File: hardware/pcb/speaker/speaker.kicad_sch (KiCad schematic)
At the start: 64 parts, among them J1 Conn_01x03, J2 Conn_01x03, J3 Conn_01x03, J4 Conn_01x03, J5 Conn_01x03, J6 Conn_01x03, J7 Conn_01x02, M1 Ultrasonic_Transducer, M10 Ultrasonic_Transducer, M11 Ultrasonic_Transducer, M12 Ultrasonic_Transducer, M13 Ultrasonic_Transducer, M14 Ultrasonic_Transducer, M15 Ultrasonic_Transducer, M16 Ultrasonic_Transducer, M17 Ultrasonic_Transducer, M18 Ultrasonic_Transducer, M19 Ultrasonic_Transducer, M2 Ultrasonic_Transducer, M3 Ultrasonic_Transducer, M4 Ultrasonic_Transducer, M5 Ultrasonic_Transducer, M6 Ultrasonic_Transducer, M7 Ultrasonic_Transducer, M8 Ultrasonic_Transducer, M9 Ultrasonic_Transducer, Q1 BC847, Q2 BC857, U1 LTC2640-Z, U2 LM2735XMF

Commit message: UPDATE BOM
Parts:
- C3: footprint Capacitor_SMD:C_0805_2012Metric_Pad1.18x1.45mm_HandSolder -> Capacitor_SMD:C_1206_3216Metric_Pad1.33x1.80mm_HandSolder
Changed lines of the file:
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@@
       (effects (font (size 1.27 1.27)) (justify left))
     )
-    (property "Footprint" "Capacitor_SMD:C_0805_2012Metric_Pad1.18x1.45mm_HandSolder" (id 2) (at 228.9302 44.45 0)
+    (property "Footprint" "Capacitor_SMD:C_1206_3216Metric_Pad1.33x1.80mm_HandSolder" (id 2) (at 228.9302 44.45 0)
       (effects (font (size 1.27 1.27)) hide)
     )
@@
     )
     (path "/892dde4e-ed28-44fe-b351-6562be659b5d"
-      (reference "C3") (unit 1) (value "10uF") (footprint "Capacitor_SMD:C_0805_2012Metric_Pad1.18x1.45mm_HandSolder")
+      (reference "C3") (unit 1) (value "10uF") (footprint "Capacitor_SMD:C_1206_3216Metric_Pad1.33x1.80mm_HandSolder")
     )
     (path "/00c022b6-5651-4944-967b-0fe8d06eb7e0"

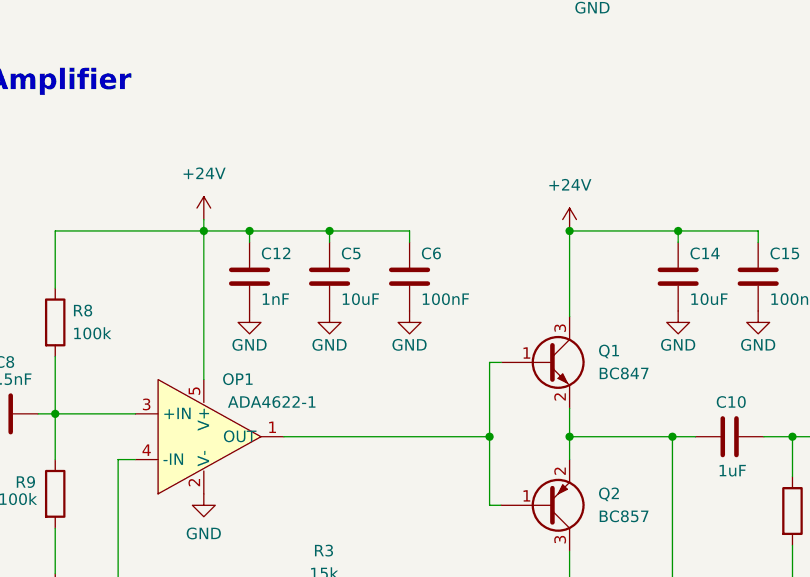
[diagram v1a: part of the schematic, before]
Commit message: rework pcb mount model
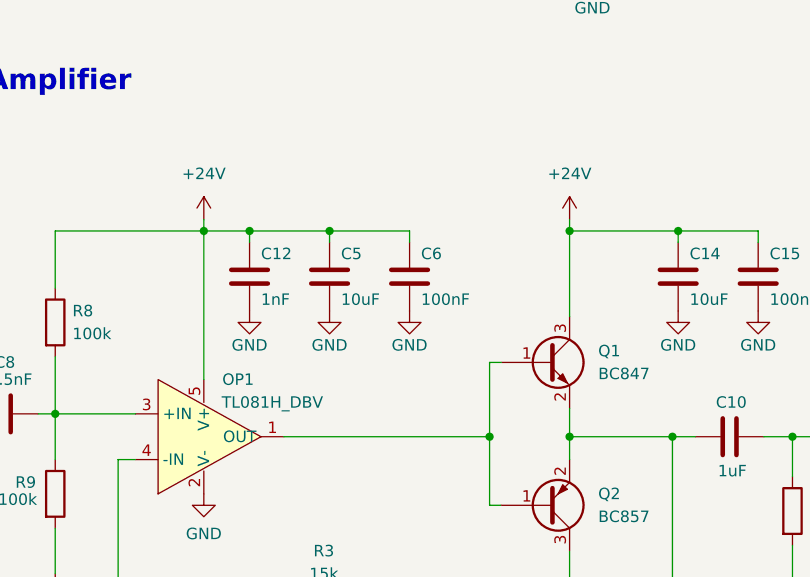
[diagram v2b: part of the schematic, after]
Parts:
- OP1: value ADA4622-1 -> TL081H_DBV
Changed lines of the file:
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@@
+    (stroke (width 0) (type default) (color 0 0 0 0))
+  )
+  (wire (pts (xy 92.075 94.615) (xy 92.075 95.885))
     (stroke (width 0) (type default) (color 0 0 0 0))
   )
@@
     (pin "1")
   )
-  (symbol (lib_id "power:+24V") (at 92.075 95.885 0) (unit 1)
-    (in_bom yes) (on_board yes) (fields_autoplaced)
-    (property "Reference" "#PWR01" (id 0) (at 92.075 99.695 0)
-      (effects (font (size 1.27 1.27)) hide)
-    )
-    (property "Value" "+24V" (id 1) (at 92.075 90.805 0))
-    (property "Footprint" "" (id 2) (at 92.075 95.885 0)
-      (effects (font (size 1.27 1.27)) hide)
-    )
-    (property "Datasheet" "" (id 3) (at 92.075 95.885 0)
+  (symbol (lib_id "power:+24V") (at 92.075 94.615 0) (unit 1)
+    (in_bom yes) (on_board yes) (fields_autoplaced)
+    (property "Reference" "#PWR01" (id 0) (at 92.075 98.425 0)
+      (effects (font (size 1.27 1.27)) hide)
+    )
+    (property "Value" "+24V" (id 1) (at 92.075 89.535 0))
+    (property "Footprint" "" (id 2) (at 92.075 94.615 0)
+      (effects (font (size 1.27 1.27)) hide)
+    )
+    (property "Datasheet" "" (id 3) (at 92.075 94.615 0)
       (effects (font (size 1.27 1.27)) hide)
     )
@@
     (in_bom yes) (on_board yes)
     (property "Reference" "OP1" (id 0) (at 55.245 112.395 0))
-    (property "Value" "ADA4622-1" (id 1) (at 59.055 114.935 0))
+    (property "Value" "TL081H_DBV" (id 1) (at 59.055 114.935 0))
     (property "Footprint" "Package_TO_SOT_SMD:SOT-23-5_HandSoldering" (id 2) (at 51.435 118.745 0)
       (effects (font (size 1.27 1.27)) hide)
@@
     )
     (path "/bf724a73-ae1d-4c58-a50e-18191201ed32"
-      (reference "OP1") (unit 1) (value "ADA4622-1") (footprint "Package_TO_SOT_SMD:SOT-23-5_HandSoldering")
+      (reference "OP1") (unit 1) (value "TL081H_DBV") (footprint "Package_TO_SOT_SMD:SOT-23-5_HandSoldering")
     )
     (path "/a413879d-4165-41a0-9ee5-56c96b82c853"

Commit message: test software
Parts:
- R4: value 5k -> 5.1k
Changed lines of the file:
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@@
       (effects (font (size 1.27 1.27)) (justify left))
     )
-    (property "Value" "5k" (id 1) (at 44.45 144.7799 0)
+    (property "Value" "5.1k" (id 1) (at 44.45 144.7799 0)
       (effects (font (size 1.27 1.27)) (justify left))
     )
@@
     )
     (path "/1392ace3-2479-46d2-8430-41ba34a5a919"
-      (reference "R4") (unit 1) (value "5k") (footprint "Resistor_SMD:R_0805_2012Metric_Pad1.20x1.40mm_HandSolder")
+      (reference "R4") (unit 1) (value "5.1k") (footprint "Resistor_SMD:R_0805_2012Metric_Pad1.20x1.40mm_HandSolder")
     )
     (path "/d3ec3927-2308-464a-86ac-ddba9a8eef92"
